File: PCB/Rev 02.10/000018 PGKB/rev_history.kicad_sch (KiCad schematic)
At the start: 0 parts

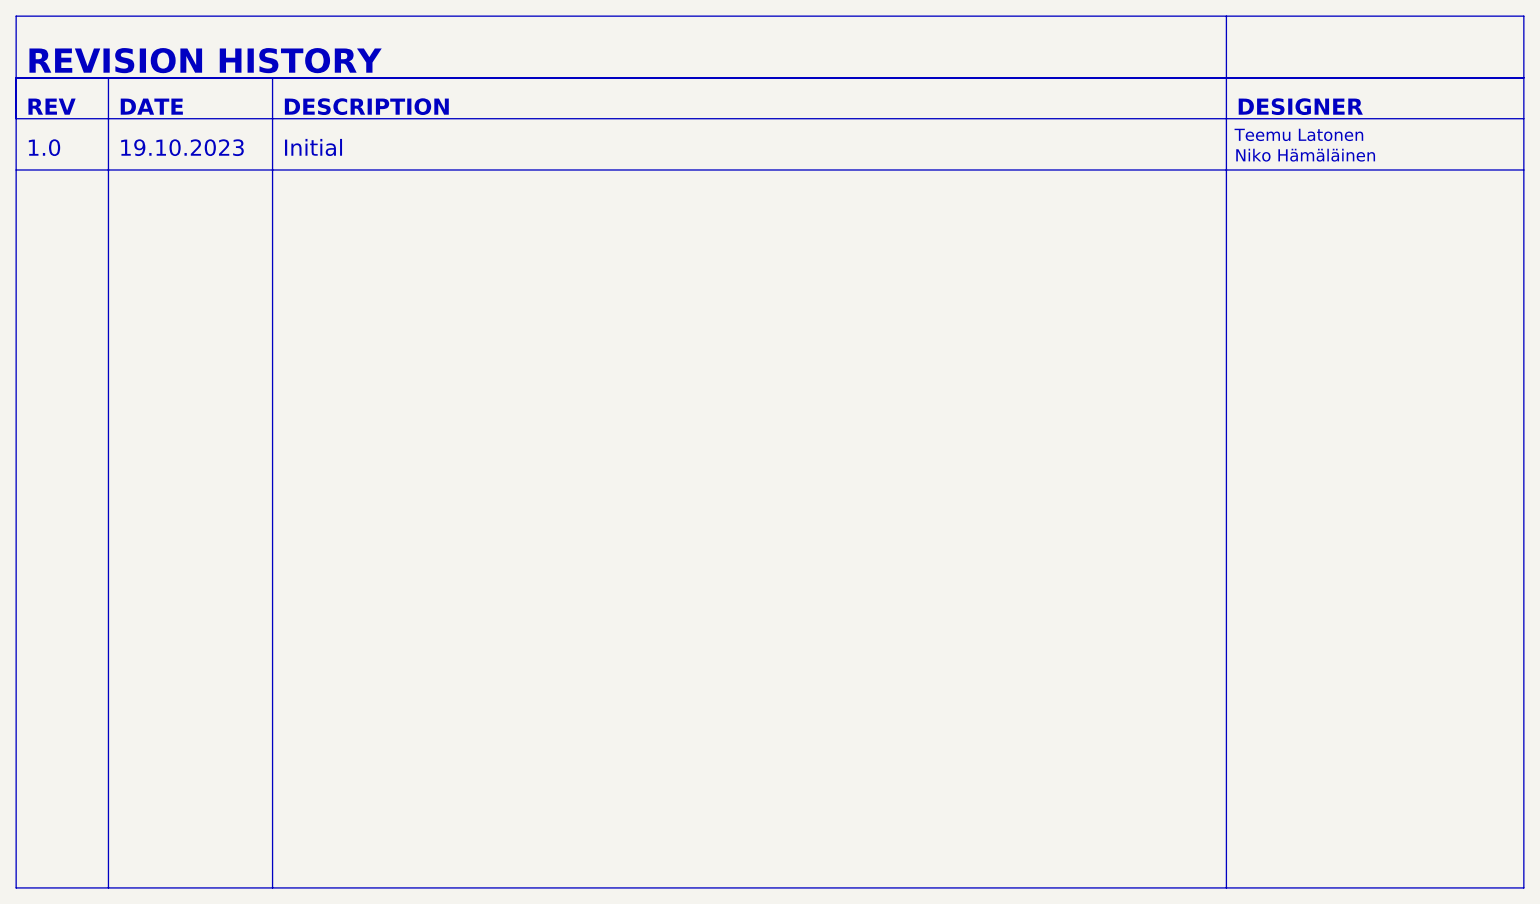
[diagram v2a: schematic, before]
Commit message: Bugfixes for Rev 2
Oscillator, USB reversed, USB series resistors values
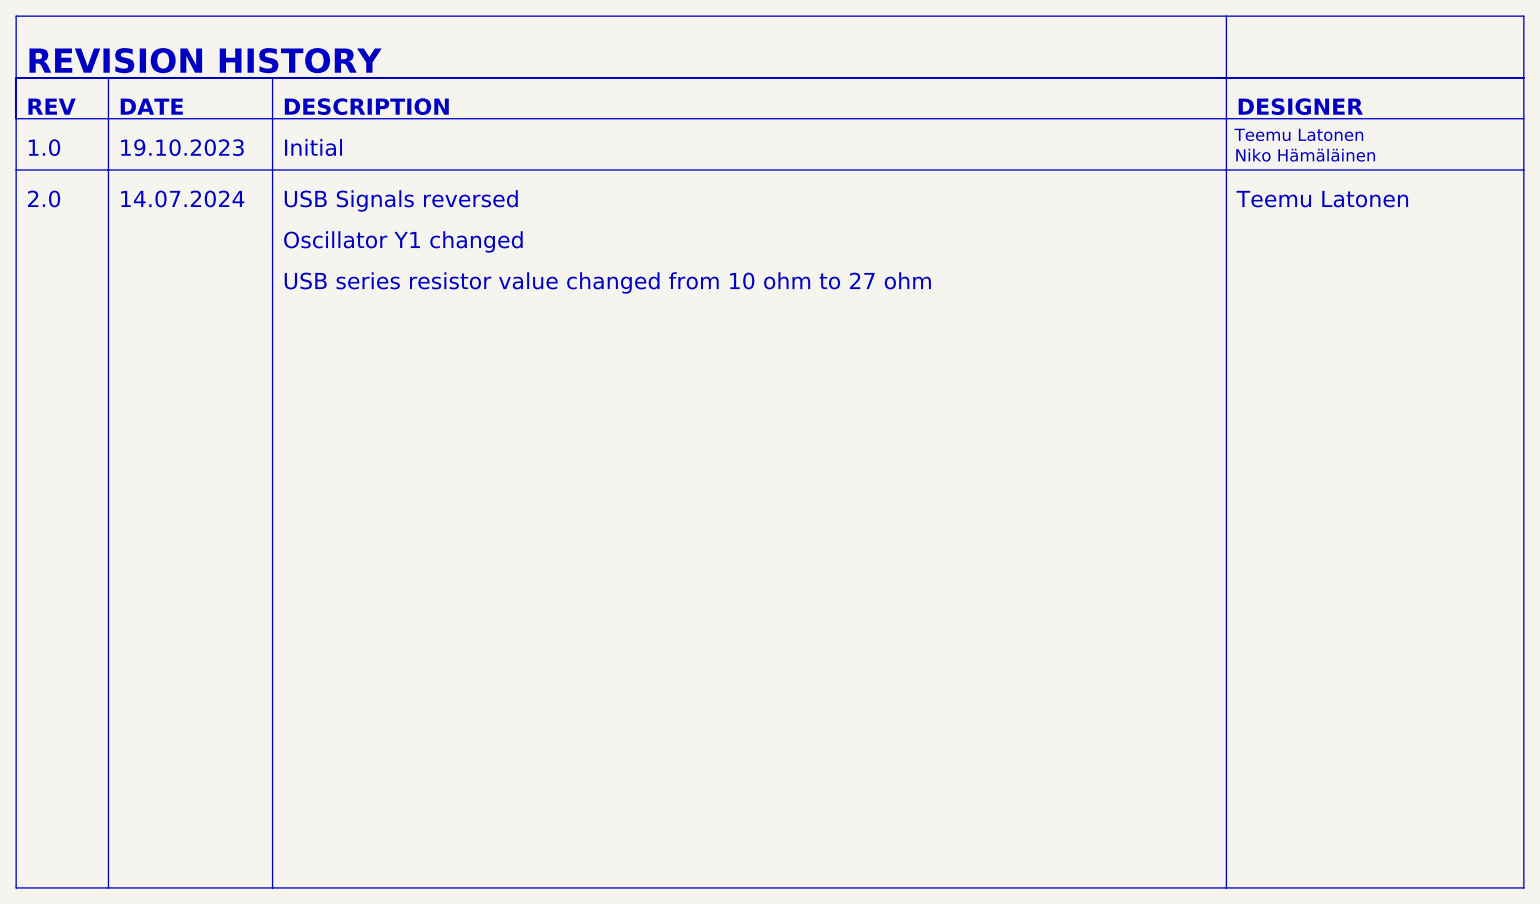
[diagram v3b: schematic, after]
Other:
- note added: "14.07.2024"
- note added: "2.0"
- note added: "Oscillator Y1 changed"
- note added: "USB Signals reversed"
- note added: "USB series resistor value changed from 10 ohm to 27 ohm"
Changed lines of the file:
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@@
+		)
+	)
+	(text "Teemu Latonen"
+		(exclude_from_sim no)
+		(at 208.28 64.77 0)
+		(effects
+			(font
+				(size 2 2)
+			)
+			(justify left bottom)
+		)
+	)
+	(text "14.07.2024"
+		(exclude_from_sim no)
+		(at 69.85 64.77 0)
+		(effects
+			(font
+				(size 2 2)
+			)
+			(justify left bottom)
 		)
 	)
@@
 		)
 	)
+	(text "2.0"
+		(exclude_from_sim no)
+		(at 58.42 64.77 0)
+		(effects
+			(font
+				(size 2 2)
+			)
+			(justify left bottom)
+		)
+	)
 	(text "DESIGNER"
 		(exclude_from_sim no)
@@
 		)
 	)
+	(text "USB series resistor value changed from 10 ohm to 27 ohm"
+		(exclude_from_sim no)
+		(at 90.17 74.93 0)
+		(effects
+			(font
+				(size 2 2)
+			)
+			(justify left bottom)
+		)
+	)
 	(text "Teemu Latonen"
 		(exclude_from_sim no)
@@
 			)
 			(justify left bottom)
+		)
+	)
+	(text "USB Signals reversed"
+		(exclude_from_sim no)
+		(at 90.17 64.77 0)
+		(effects
+			(font
+				(size 2 2)
+			)
+			(justify left bottom)
+		)
+	)
+	(text "Oscillator Y1 changed"
+		(exclude_from_sim no)
+		(at 90.17 69.85 0)
+		(effects
+			(font
+				(size 2 2)
+			)
+			(justify left bottom)
